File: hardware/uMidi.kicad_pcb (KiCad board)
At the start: 2 copper layers, 66 x 40.6 mm, 59 parts, among them CON1 USB-MINI-B, IC1 ATXMEGA128A4U-M, IC2 74LS14, IC3 LT1129CST-3.3, IC4 6N138, P1 MIDI In, P2 MIDI Thru, P3 MIDI T/O, P4 MIDI Out, P5 5..12 V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

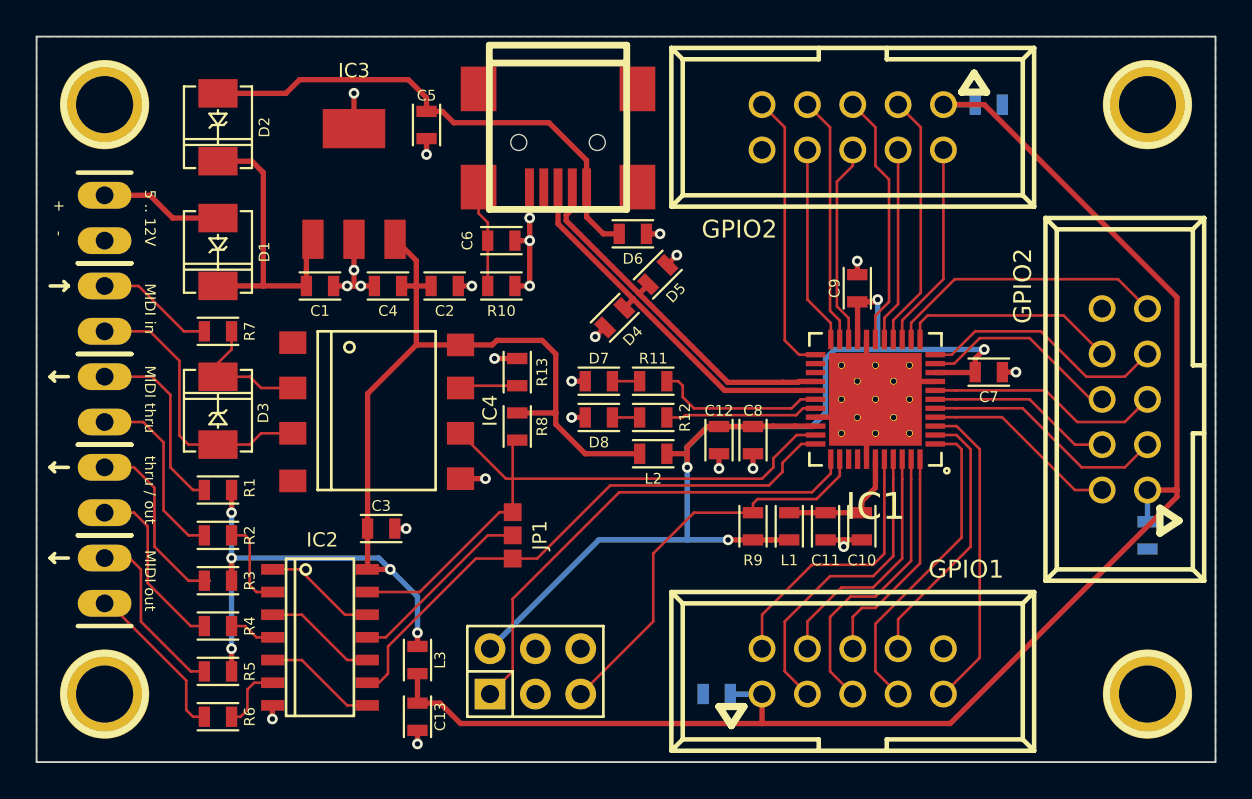
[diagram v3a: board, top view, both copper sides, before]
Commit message: Add some redundancy vias
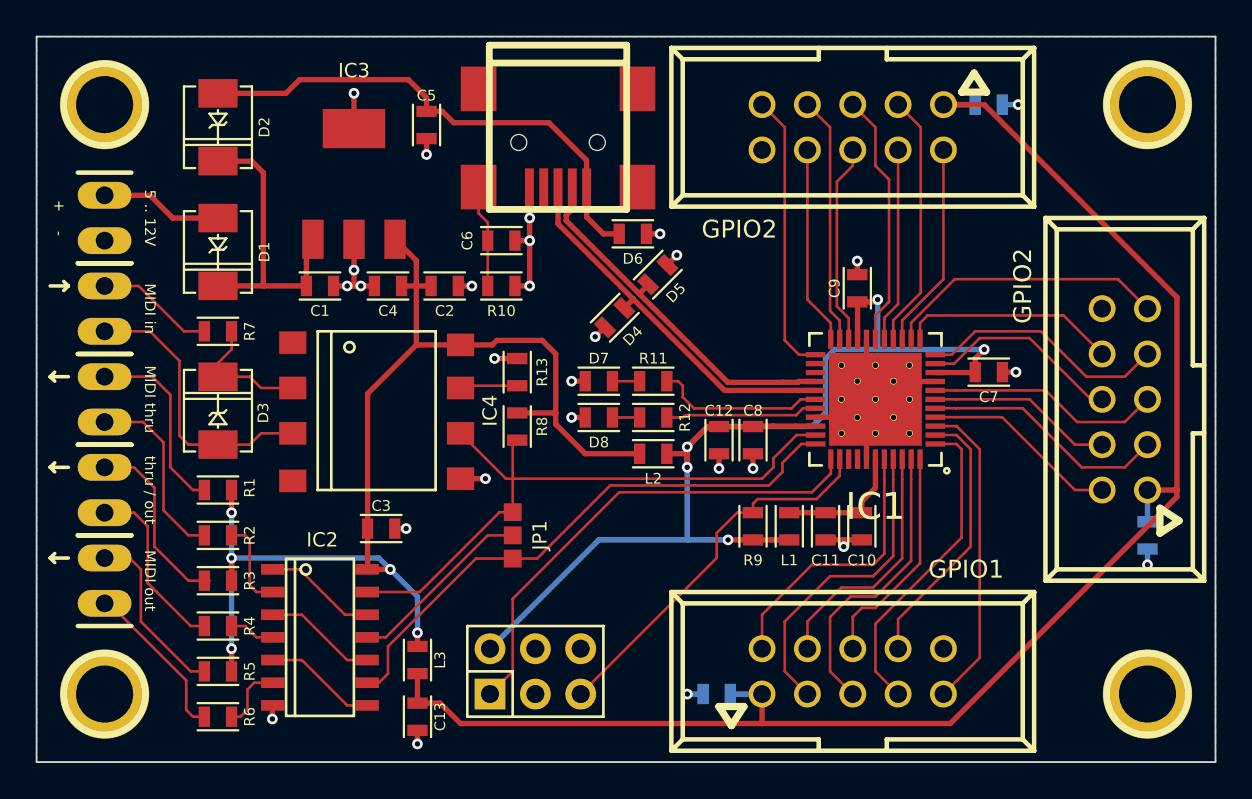
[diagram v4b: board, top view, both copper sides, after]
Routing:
- net GND: track 44.5 -> 47.2 mm, vias 24 -> 27
- net Net-(IC1-Pad35): track 23.0 -> 21.6 mm
- net Net-(C12-Pad1): track 65.2 -> 66.4 mm, vias 4 -> 5
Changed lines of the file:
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@@
     (thickness 1.6)
     (drawings 22)
-    (tracks 477)
+    (tracks 485)
     (zones 0)
     (modules 59)
@@
   (segment (start 82.41792 137.15492) (end 82.423 137.16) (width 0.3) (layer F.Cu) (net 1))
   (segment (start 82.588 134.747) (end 82.79 134.545) (width 0.3) (layer F.Cu) (net 1) (status 30))
+  (segment (start 121.412 127) (end 122.301 127) (width 0.3) (layer B.Cu) (net 2))
+  (via (at 122.301 127) (size 0.6) (layers F.Cu B.Cu) (net 2))
+  (segment (start 129.54 151.892) (end 129.54 152.781) (width 0.3) (layer B.Cu) (net 2))
+  (via (at 129.54 152.781) (size 0.6) (layers F.Cu B.Cu) (net 2))
+  (segment (start 104.648 160.02) (end 103.759 160.02) (width 0.3) (layer B.Cu) (net 2))
+  (via (at 103.759 160.02) (size 0.6) (layers F.Cu B.Cu) (net 2))
   (segment (start 88.646 162.052) (end 88.646 162.814) (width 0.3) (layer F.Cu) (net 2))
   (via (at 88.646 162.814) (size 0.6) (layers F.Cu B.Cu) (net 2))
@@
   (segment (start 114.3 148.01) (end 114.3 148.463) (width 0.3) (layer F.Cu) (net 4))
   (segment (start 114.3 148.463) (end 113.538 149.225) (width 0.3) (layer F.Cu) (net 4))
+  (segment (start 103.759 147.32) (end 103.759 146.177) (width 0.3) (layer B.Cu) (net 5))
+  (via (at 103.759 146.177) (size 0.6) (layers F.Cu B.Cu) (net 5))
   (segment (start 103.759 151.384) (end 98.806 151.384) (width 0.3) (layer B.Cu) (net 5))
   (segment (start 98.806 151.384) (end 92.71 157.48) (width 0.3) (layer B.Cu) (net 5))
@@
   (segment (start 113.284 138.049) (end 114.3 138.049) (width 0.3) (layer F.Cu) (net 5))
   (segment (start 103.759 146.177) (end 104.902 145.034) (width 0.3) (layer B.Cu) (net 5))
-  (segment (start 103.759 147.32) (end 103.759 146.177) (width 0.3) (layer B.Cu) (net 5))
   (segment (start 112.014 140.716) (end 114.427 140.716) (width 0.3) (layer B.Cu) (net 5))
   (segment (start 111.506 141.224) (end 112.014 140.716) (width 0.3) (layer B.Cu) (net 5))
@@
   (segment (start 110.744 145.034) (end 111.506 144.272) (width 0.3) (layer B.Cu) (net 5))
   (segment (start 104.902 145.034) (end 110.744 145.034) (width 0.3) (layer B.Cu) (net 5))
+  (segment (start 103.759 147.32) (end 103.759 146.177) (width 0.3) (layer B.Cu) (net 5) (status 2))
   (segment (start 109.1057 142.5575) (end 109.9566 142.5575) (width 0.3) (layer F.Cu) (net 6))
   (segment (start 110.0041 142.51) (end 110.95 142.51) (width 0.3) (layer F.Cu) (net 6))
@@
   (segment (start 93.98 154.686) (end 99.949 148.717) (width 0.15) (layer F.Cu) (net 38))
   (segment (start 93.98 158.75) (end 93.98 154.686) (width 0.15) (layer F.Cu) (net 38))
-  (segment (start 97.79 160.02) (end 101.854 155.956) (width 0.15) (layer F.Cu) (net 39))
-  (segment (start 104.14 149.86) (end 107.442 149.86) (width 0.15) (layer F.Cu) (net 39))
-  (segment (start 101.854 152.146) (end 104.14 149.86) (width 0.15) (layer F.Cu) (net 39))
-  (segment (start 101.854 155.956) (end 101.854 152.146) (width 0.15) (layer F.Cu) (net 39))
+  (segment (start 97.79 160.02) (end 105.41 152.4) (width 0.15) (layer F.Cu) (net 39))
+  (segment (start 106.553 149.86) (end 107.442 149.86) (width 0.15) (layer F.Cu) (net 39))
+  (segment (start 105.41 151.003) (end 106.553 149.86) (width 0.15) (layer F.Cu) (net 39))
+  (segment (start 105.41 152.4) (end 105.41 151.003) (width 0.15) (layer F.Cu) (net 39))
   (segment (start 112.3 147.796) (end 110.998 149.098) (width 0.15) (layer F.Cu) (net 39))
   (segment (start 110.998 149.098) (end 107.696 149.098) (width 0.15) (layer F.Cu) (net 39))

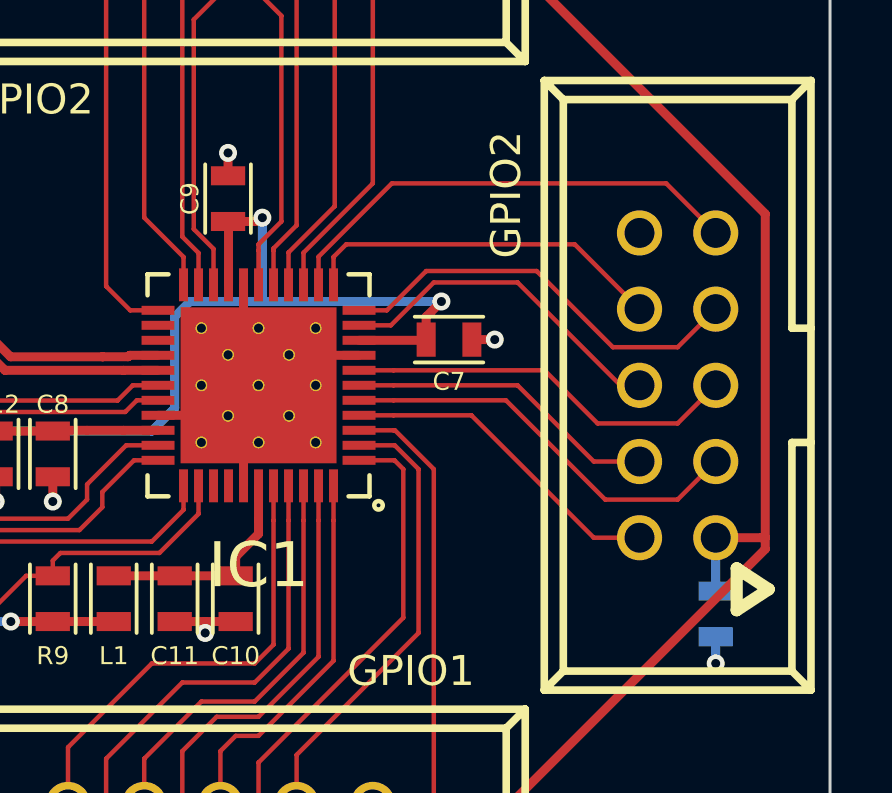
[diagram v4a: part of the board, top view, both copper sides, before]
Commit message: Add TWI pullup resistors
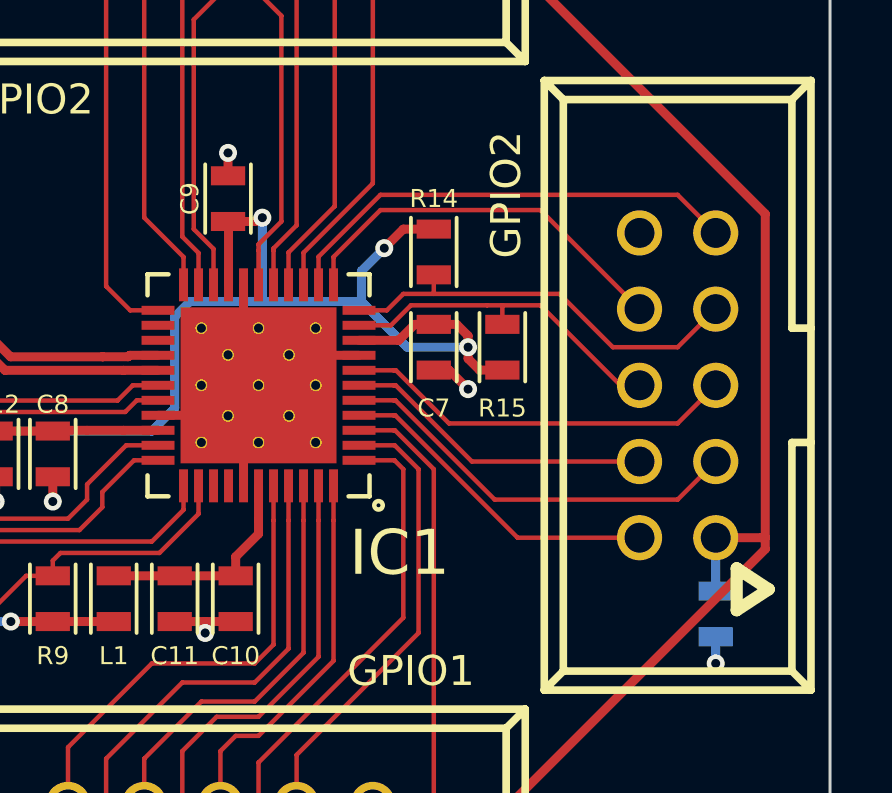
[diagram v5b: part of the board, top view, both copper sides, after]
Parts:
- added R14: 10k, SMD:SMD-0603, F.Cu at (120.1, 139.1)
- added R15: 10k, SMD:SMD-0603, F.Cu at (122.4, 142.2)
- moved C7 0.57 mm to (120.1, 142.2), turned to 270 degrees
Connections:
- net Net-(C12-Pad1) renamed PWR_MCU
- net Net-(IC1-Pad10) renamed SDA
- net Net-(IC1-Pad11) renamed SCL
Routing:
- net PWR_MCU: track 66.4 -> 74.2 mm, vias 5 -> 6
- net Net-(IC1-Pad12): track 12.2 -> 13.1 mm
- net GND: track 47.2 -> 47.8 mm

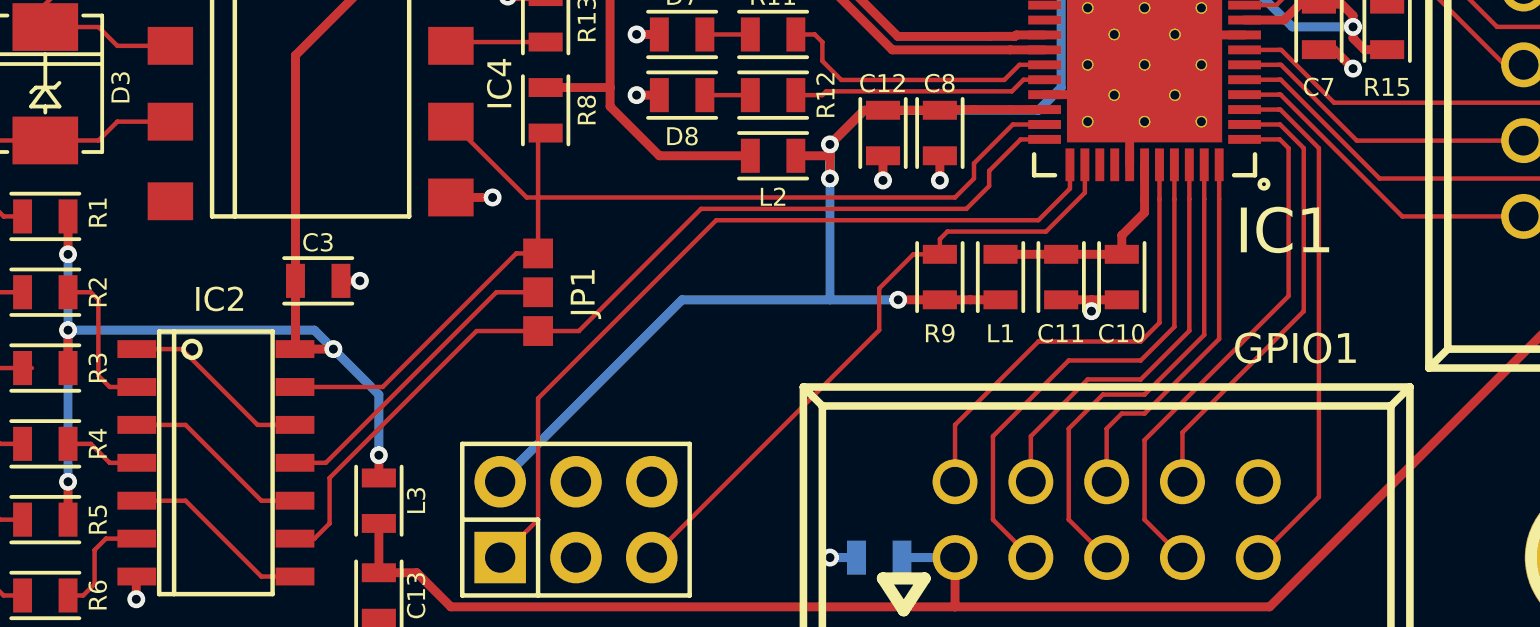
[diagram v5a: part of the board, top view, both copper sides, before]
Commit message: Add labels to jumper
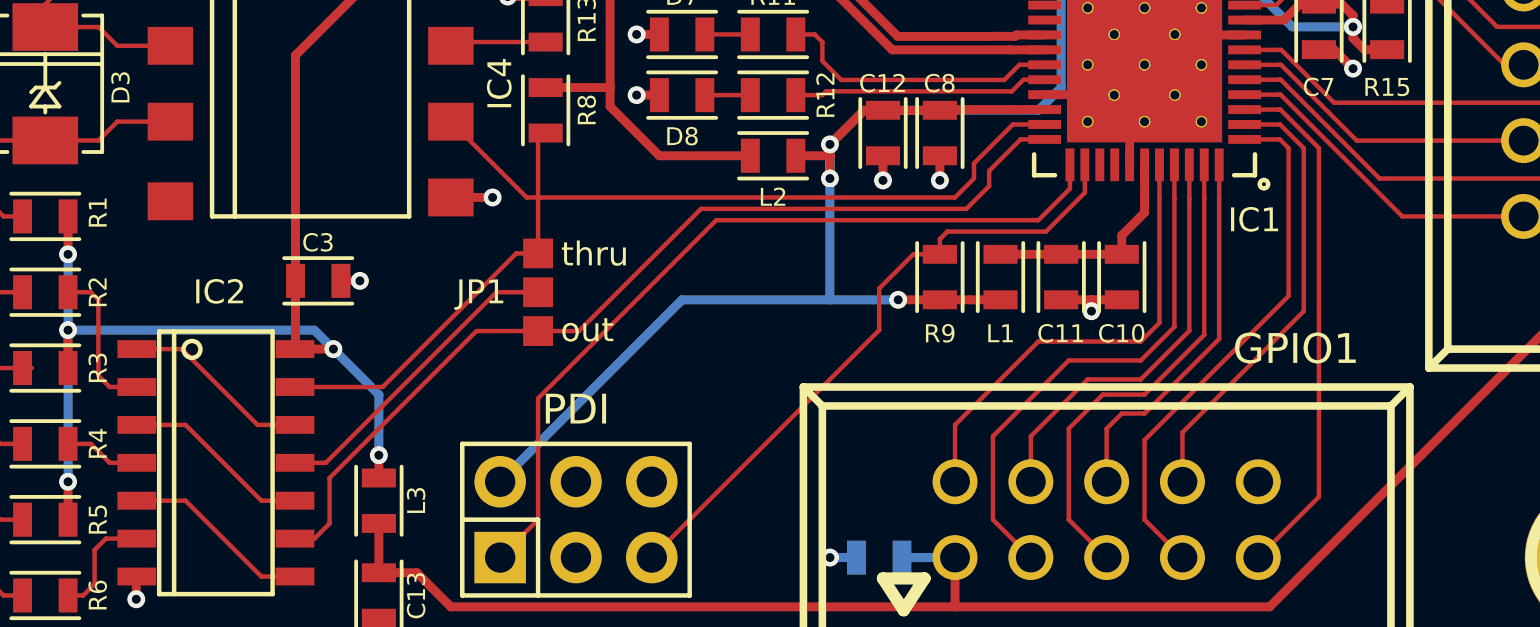
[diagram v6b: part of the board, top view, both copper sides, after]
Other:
- board text added: "out"
- board text added: "thru"
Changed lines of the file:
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@@
     (area 67.259999 123.139999 133.400001 163.880001)
     (thickness 1.6)
-    (drawings 22)
+    (drawings 24)
     (tracks 503)
     (zones 0)
@@
   (module Solderjumper:SJ3 placed (layer F.Cu)
     (at 93.98 151.13 270)
-    (fp_text reference JP1 (at 0 -1.524 270) (layer F.SilkS)
+    (fp_text reference JP1 (at 0 1.905 360) (layer F.SilkS)
       (effects (font (size 0.8 0.8) (thickness 0.15)))
     )
@@
       (effects (font (size 1.27 1.27) (thickness 0.2032)))
     )
-    (fp_text value PDI (at 0 0) (layer F.SilkS) hide
-      (effects (font (size 1.27 1.27) (thickness 0.2032)))
+    (fp_text value PDI (at 0 -3.683) (layer F.SilkS)
+      (effects (font (size 1 1) (thickness 0.2)))
     )
     (fp_line (start -3.81 0) (end -1.27 0) (layer F.SilkS) (width 0.15))
@@
     (tags "QFN VQFN")
     (attr smd)
-    (fp_text reference IC1 (at -4.699 -5.588 180) (layer F.SilkS)
-      (effects (font (size 1.5 1.5) (thickness 0.15)))
+    (fp_text reference IC1 (at -3.683 -5.207 180) (layer F.SilkS)
+      (effects (font (size 0.8 0.8) (thickness 0.15)))
     )
     (fp_text value ATXMEGA128A4U-M (at 0 6 180) (layer F.SilkS) hide
@@
     (tags "CMS SOJ")
     (attr smd)
-    (fp_text reference IC2 (at -5.461 -0.127 360) (layer F.SilkS)
+    (fp_text reference IC2 (at -5.715 -0.127 360) (layer F.SilkS)
       (effects (font (size 0.8 0.8) (thickness 0.15)))
     )
@@
     )
   )
+  (gr_text out (at 95.631 152.4) (layer F.SilkS)
+    (effects (font (size 0.8 0.8) (thickness 0.15)))
+  )
+  (gr_text thru (at 95.885 149.86) (layer F.SilkS)
+    (effects (font (size 0.8 0.8) (thickness 0.15)))
+  )
   (gr_line (start 68.072 152.4) (end 68.326 152.654) (angle 90) (layer F.SilkS) (width 0.2))
